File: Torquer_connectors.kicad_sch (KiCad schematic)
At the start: 0 parts

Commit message: eeprom fanned out
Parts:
- added JT1, JT2, JT3: 502352-0210, symbol 502352-0210:502352-0210
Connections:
- new net GND: JT1.MP1, JT1.MP2, JT2.MP1, JT2.MP2, JT3.MP1, JT3.MP2
- new net MT2_Out1: JT2.1
- new net MT2_Out2: JT2.2
- new net MT3_Out1: JT3.1
- new net MT3_Out2: JT3.2
- new net MT_Out1: JT1.1
- new net MT_Out2: JT1.2
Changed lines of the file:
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@@
 (kicad_sch (version 20211123) (generator eeschema)
   (paper "A4")
+  (junction (at 36.83 58.42) (diameter 0) (color 0 0 0 0)
+  )
+  (junction (at 35.56 34.29) (diameter 0) (color 0 0 0 0)
+  )
+  (junction (at 39.37 85.09) (diameter 0) (color 0 0 0 0)
+  )
+  (wire (pts (xy 39.37 85.09) (xy 39.37 87.63))
+    (stroke (width 0) (type default) (color 0 0 0 0))
+  )
+  (wire (pts (xy 36.83 58.42) (xy 39.37 58.42))
+    (stroke (width 0) (type default) (color 0 0 0 0))
+  )
+  (wire (pts (xy 35.56 34.29) (xy 39.37 34.29))
+    (stroke (width 0) (type default) (color 0 0 0 0))
+  )
+  (wire (pts (xy 39.37 31.75) (xy 35.56 31.75))
+    (stroke (width 0) (type default) (color 0 0 0 0))
+  )
+  (wire (pts (xy 36.83 58.42) (xy 36.83 62.23))
+    (stroke (width 0) (type default) (color 0 0 0 0))
+  )
+  (wire (pts (xy 39.37 85.09) (xy 40.64 85.09))
+    (stroke (width 0) (type default) (color 0 0 0 0))
+  )
+  (wire (pts (xy 35.56 31.75) (xy 35.56 34.29))
+    (stroke (width 0) (type default) (color 0 0 0 0))
+  )
+  (wire (pts (xy 40.64 82.55) (xy 39.37 82.55))
+    (stroke (width 0) (type default) (color 0 0 0 0))
+  )
+  (wire (pts (xy 36.83 55.88) (xy 36.83 58.42))
+    (stroke (width 0) (type default) (color 0 0 0 0))
+  )
+  (wire (pts (xy 39.37 82.55) (xy 39.37 85.09))
+    (stroke (width 0) (type default) (color 0 0 0 0))
+  )
+  (wire (pts (xy 39.37 55.88) (xy 36.83 55.88))
+    (stroke (width 0) (type default) (color 0 0 0 0))
+  )
+  (wire (pts (xy 35.56 34.29) (xy 35.56 35.56))
+    (stroke (width 0) (type default) (color 0 0 0 0))
+  )
+  (hierarchical_label "MT_Out1" (shape input) (at 62.23 31.75 0)
+    (effects (font (size 1.27 1.27)) (justify left))
+  )
+  (hierarchical_label "MT3_Out1" (shape input) (at 63.5 82.55 0)
+    (effects (font (size 1.27 1.27)) (justify left))
+  )
+  (hierarchical_label "MT2_Out1" (shape input) (at 62.23 55.88 0)
+    (effects (font (size 1.27 1.27)) (justify left))
+  )
+  (hierarchical_label "MT_Out2" (shape input) (at 62.23 34.29 0)
+    (effects (font (size 1.27 1.27)) (justify left))
+  )
+  (hierarchical_label "MT3_Out2" (shape input) (at 63.5 85.09 0)
+    (effects (font (size 1.27 1.27)) (justify left))
+  )
+  (hierarchical_label "MT2_Out2" (shape input) (at 62.23 58.42 0)
+    (effects (font (size 1.27 1.27)) (justify left))
+  )
+  (symbol (lib_id "power:GND") (at 36.83 62.23 0) (unit 1)
+    (in_bom yes) (on_board yes) (fields_autoplaced)
+    (property "Reference" "#PWR?" (id 0) (at 36.83 68.58 0)
+      (effects (font (size 1.27 1.27)) hide)
+    )
+    (property "Value" "GND" (id 1) (at 36.83 67.31 0))
+    (property "Footprint" "" (id 2) (at 36.83 62.23 0)
+      (effects (font (size 1.27 1.27)) hide)
+    )
+    (property "Datasheet" "" (id 3) (at 36.83 62.23 0)
+      (effects (font (size 1.27 1.27)) hide)
+    )
+    (pin "1")
+  )
+  (symbol (lib_id "502352-0210:502352-0210") (at 39.37 55.88 0) (unit 1)
+    (in_bom yes) (on_board yes) (fields_autoplaced)
+    (property "Reference" "JT2" (id 0) (at 50.8 43.18 0))
+    (property "Value" "502352-0210" (id 1) (at 50.8 45.72 0))
+    (property "Footprint" "" (id 2) (at 39.37 55.88 0)
+      (effects (font (size 1.27 1.27)) hide)
+    )
+    (property "Datasheet" "" (id 3) (at 39.37 55.88 0)
+      (effects (font (size 1.27 1.27)) hide)
+    )
+    (property "Reference_1" "J" (id 4) (at 50.8 48.26 0))
+    (property "Value_1" "502352-0210" (id 5) (at 50.8 50.8 0))
+    (property "Footprint_1" "5023520210" (id 6) (at 58.42 150.8 0)
+      (effects (font (size 1.27 1.27)) (justify left top) hide)
+    )
+    (property "Datasheet_1" "https://componentsearchengine.com/Datasheets/1/502352-0210.pdf" (id 7) (at 58.42 250.8 0)
+      (effects (font (size 1.27 1.27)) (justify left top) hide)
+    )
+    (property "Height" "6.4" (id 8) (at 58.42 450.8 0)
+      (effects (font (size 1.27 1.27)) (justify left top) hide)
+    )
+    (property "Mouser Part Number" "538-502352-0210" (id 9) (at 58.42 550.8 0)
+      (effects (font (size 1.27 1.27)) (justify left top) hide)
+    )
+    (property "Mouser Price/Stock" "https://www.mouser.co.uk/ProductDetail/Molex/502352-0210?qs=yd8XiKYcH9lys38VlWdUCA%3D%3D" (id 10) (at 58.42 650.8 0)
+      (effects (font (size 1.27 1.27)) (justify left top) hide)
+    )
+    (property "Manufacturer_Name" "Molex" (id 11) (at 58.42 750.8 0)
+      (effects (font (size 1.27 1.27)) (justify left top) hide)
+    )
+    (property "Manufacturer_Part_Number" "502352-0210" (id 12) (at 58.42 850.8 0)
+      (effects (font (size 1.27 1.27)) (justify left top) hide)
+    )
+    (pin "1")
+    (pin "2")
+    (pin "MP1")
+    (pin "MP2")
+  )
+  (symbol (lib_id "power:GND") (at 39.37 87.63 0) (unit 1)
+    (in_bom yes) (on_board yes) (fields_autoplaced)
+    (property "Reference" "#PWR?" (id 0) (at 39.37 93.98 0)
+      (effects (font (size 1.27 1.27)) hide)
+    )
+    (property "Value" "GND" (id 1) (at 39.37 92.71 0))
+    (property "Footprint" "" (id 2) (at 39.37 87.63 0)
+      (effects (font (size 1.27 1.27)) hide)
+    )
+    (property "Datasheet" "" (id 3) (at 39.37 87.63 0)
+      (effects (font (size 1.27 1.27)) hide)
+    )
+    (pin "1")
+  )
+  (symbol (lib_id "502352-0210:502352-0210") (at 39.37 31.75 0) (unit 1)
+    (in_bom yes) (on_board yes) (fields_autoplaced)
+    (property "Reference" "JT1" (id 0) (at 50.8 19.05 0))
+    (property "Value" "502352-0210" (id 1) (at 50.8 21.59 0))
+    (property "Footprint" "" (id 2) (at 39.37 31.75 0)
+      (effects (font (size 1.27 1.27)) hide)
+    )
+    (property "Datasheet" "" (id 3) (at 39.37 31.75 0)
+      (effects (font (size 1.27 1.27)) hide)
+    )
+    (property "Reference_1" "J" (id 4) (at 50.8 24.13 0))
+    (property "Value_1" "502352-0210" (id 5) (at 50.8 26.67 0))
+    (property "Footprint_1" "5023520210" (id 6) (at 58.42 126.67 0)
+      (effects (font (size 1.27 1.27)) (justify left top) hide)
+    )
+    (property "Datasheet_1" "https://componentsearchengine.com/Datasheets/1/502352-0210.pdf" (id 7) (at 58.42 226.67 0)
+      (effects (font (size 1.27 1.27)) (justify left top) hide)
+    )
+    (property "Height" "6.4" (id 8) (at 58.42 426.67 0)
+      (effects (font (size 1.27 1.27)) (justify left top) hide)
+    )
+    (property "Mouser Part Number" "538-502352-0210" (id 9) (at 58.42 526.67 0)
+      (effects (font (size 1.27 1.27)) (justify left top) hide)
+    )
+    (property "Mouser Price/Stock" "https://www.mouser.co.uk/ProductDetail/Molex/502352-0210?qs=yd8XiKYcH9lys38VlWdUCA%3D%3D" (id 10) (at 58.42 626.67 0)
+      (effects (font (size 1.27 1.27)) (justify left top) hide)
+    )
+    (property "Manufacturer_Name" "Molex" (id 11) (at 58.42 726.67 0)
+      (effects (font (size 1.27 1.27)) (justify left top) hide)
+    )
+    (property "Manufacturer_Part_Number" "502352-0210" (id 12) (at 58.42 826.67 0)
+      (effects (font (size 1.27 1.27)) (justify left top) hide)
+    )
+    (pin "1")
+    (pin "2")
+    (pin "MP1")
+    (pin "MP2")
+  )
+  (symbol (lib_id "power:GND") (at 35.56 35.56 0) (unit 1)
+    (in_bom yes) (on_board yes) (fields_autoplaced)
+    (property "Reference" "#PWR?" (id 0) (at 35.56 41.91 0)
+      (effects (font (size 1.27 1.27)) hide)
+    )
+    (property "Value" "GND" (id 1) (at 35.56 40.64 0))
+    (property "Footprint" "" (id 2) (at 35.56 35.56 0)
+      (effects (font (size 1.27 1.27)) hide)
+    )
+    (property "Datasheet" "" (id 3) (at 35.56 35.56 0)
+      (effects (font (size 1.27 1.27)) hide)
+    )
+    (pin "1")
+  )
+  (symbol (lib_id "502352-0210:502352-0210") (at 40.64 82.55 0) (unit 1)
+    (in_bom yes) (on_board yes) (fields_autoplaced)
+    (property "Reference" "JT3" (id 0) (at 52.07 69.85 0))
+    (property "Value" "502352-0210" (id 1) (at 52.07 72.39 0))
+    (property "Footprint" "" (id 2) (at 40.64 82.55 0)
+      (effects (font (size 1.27 1.27)) hide)
+    )
+    (property "Datasheet" "" (id 3) (at 40.64 82.55 0)
+      (effects (font (size 1.27 1.27)) hide)
+    )
+    (property "Reference_1" "J" (id 4) (at 52.07 74.93 0))
+    (property "Value_1" "502352-0210" (id 5) (at 52.07 77.47 0))
+    (property "Footprint_1" "5023520210" (id 6) (at 59.69 177.47 0)
+      (effects (font (size 1.27 1.27)) (justify left top) hide)
+    )
+    (property "Datasheet_1" "https://componentsearchengine.com/Datasheets/1/502352-0210.pdf" (id 7) (at 59.69 277.47 0)
+      (effects (font (size 1.27 1.27)) (justify left top) hide)
+    )
+    (property "Height" "6.4" (id 8) (at 59.69 477.47 0)
+      (effects (font (size 1.27 1.27)) (justify left top) hide)
+    )
+    (property "Mouser Part Number" "538-502352-0210" (id 9) (at 59.69 577.47 0)
+      (effects (font (size 1.27 1.27)) (justify left top) hide)
+    )
+    (property "Mouser Price/Stock" "https://www.mouser.co.uk/ProductDetail/Molex/502352-0210?qs=yd8XiKYcH9lys38VlWdUCA%3D%3D" (id 10) (at 59.69 677.47 0)
+      (effects (font (size 1.27 1.27)) (justify left top) hide)
+    )
+    (property "Manufacturer_Name" "Molex" (id 11) (at 59.69 777.47 0)
+      (effects (font (size 1.27 1.27)) (justify left top) hide)
+    )
+    (property "Manufacturer_Part_Number" "502352-0210" (id 12) (at 59.69 877.47 0)
+      (effects (font (size 1.27 1.27)) (justify left top) hide)
+    )
+    (pin "1")
+    (pin "2")
+    (pin "MP1")
+    (pin "MP2")
+  )
 )

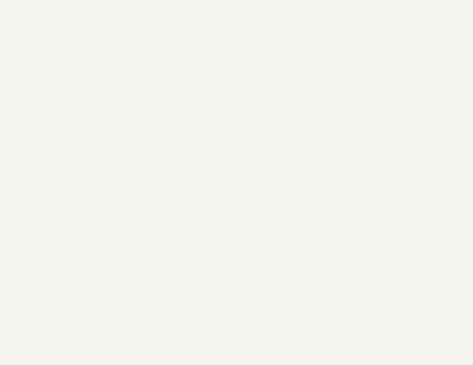
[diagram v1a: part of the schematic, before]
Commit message: MCU interfaces are done! Check the Changes and Complete ERC modifications
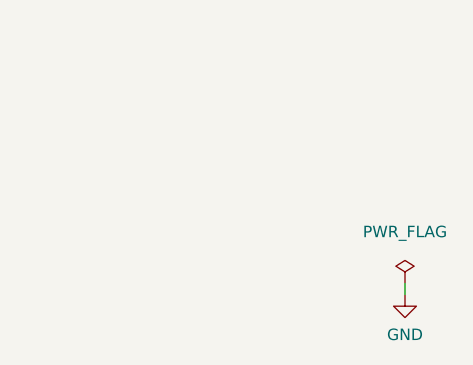
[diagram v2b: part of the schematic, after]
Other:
- company: (none) -> Parikshit Student Satellite Team
- title: (none) -> AOCS BOARD
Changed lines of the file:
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@@
 (kicad_sch (version 20211123) (generator eeschema)
   (paper "A4")
+  (title_block
+    (title "AOCS BOARD")
+    (company "Parikshit Student Satellite Team")
+  )
   (junction (at 36.83 58.42) (diameter 0) (color 0 0 0 0)
   )
@@
     (stroke (width 0) (type default) (color 0 0 0 0))
   )
+  (wire (pts (xy 260.985 143.51) (xy 260.985 142.24))
+    (stroke (width 0) (type default) (color 0 0 0 0))
+  )
   (wire (pts (xy 36.83 58.42) (xy 36.83 62.23))
     (stroke (width 0) (type default) (color 0 0 0 0))
@@
   (symbol (lib_id "power:GND") (at 36.83 62.23 0) (unit 1)
     (in_bom yes) (on_board yes) (fields_autoplaced)
-    (property "Reference" "#PWR?" (id 0) (at 36.83 68.58 0)
+    (property "Reference" "#PWR0247" (id 0) (at 36.83 68.58 0)
       (effects (font (size 1.27 1.27)) hide)
     )
@@
     )
     (property "Datasheet" "" (id 3) (at 36.83 62.23 0)
+      (effects (font (size 1.27 1.27)) hide)
+    )
+    (pin "1")
+  )
+  (symbol (lib_id "power:PWR_FLAG") (at 260.985 142.24 0) (unit 1)
+    (in_bom yes) (on_board yes) (fields_autoplaced)
+    (property "Reference" "#FLG0113" (id 0) (at 260.985 140.335 0)
+      (effects (font (size 1.27 1.27)) hide)
+    )
+    (property "Value" "PWR_FLAG" (id 1) (at 260.985 136.525 0))
+    (property "Footprint" "" (id 2) (at 260.985 142.24 0)
+      (effects (font (size 1.27 1.27)) hide)
+    )
+    (property "Datasheet" "~" (id 3) (at 260.985 142.24 0)
       (effects (font (size 1.27 1.27)) hide)
     )
@@
   (symbol (lib_id "power:GND") (at 39.37 87.63 0) (unit 1)
     (in_bom yes) (on_board yes) (fields_autoplaced)
-    (property "Reference" "#PWR?" (id 0) (at 39.37 93.98 0)
+    (property "Reference" "#PWR0245" (id 0) (at 39.37 93.98 0)
       (effects (font (size 1.27 1.27)) hide)
     )
@@
   (symbol (lib_id "power:GND") (at 35.56 35.56 0) (unit 1)
     (in_bom yes) (on_board yes) (fields_autoplaced)
-    (property "Reference" "#PWR?" (id 0) (at 35.56 41.91 0)
+    (property "Reference" "#PWR0246" (id 0) (at 35.56 41.91 0)
       (effects (font (size 1.27 1.27)) hide)
     )
@@
     (pin "MP2")
   )
+  (symbol (lib_id "power:GND") (at 260.985 143.51 0) (unit 1)
+    (in_bom yes) (on_board yes) (fields_autoplaced)
+    (property "Reference" "#PWR0277" (id 0) (at 260.985 149.86 0)
+      (effects (font (size 1.27 1.27)) hide)
+    )
+    (property "Value" "GND" (id 1) (at 260.985 147.955 0))
+    (property "Footprint" "" (id 2) (at 260.985 143.51 0)
+      (effects (font (size 1.27 1.27)) hide)
+    )
+    (property "Datasheet" "" (id 3) (at 260.985 143.51 0)
+      (effects (font (size 1.27 1.27)) hide)
+    )
+    (pin "1")
+  )
 )

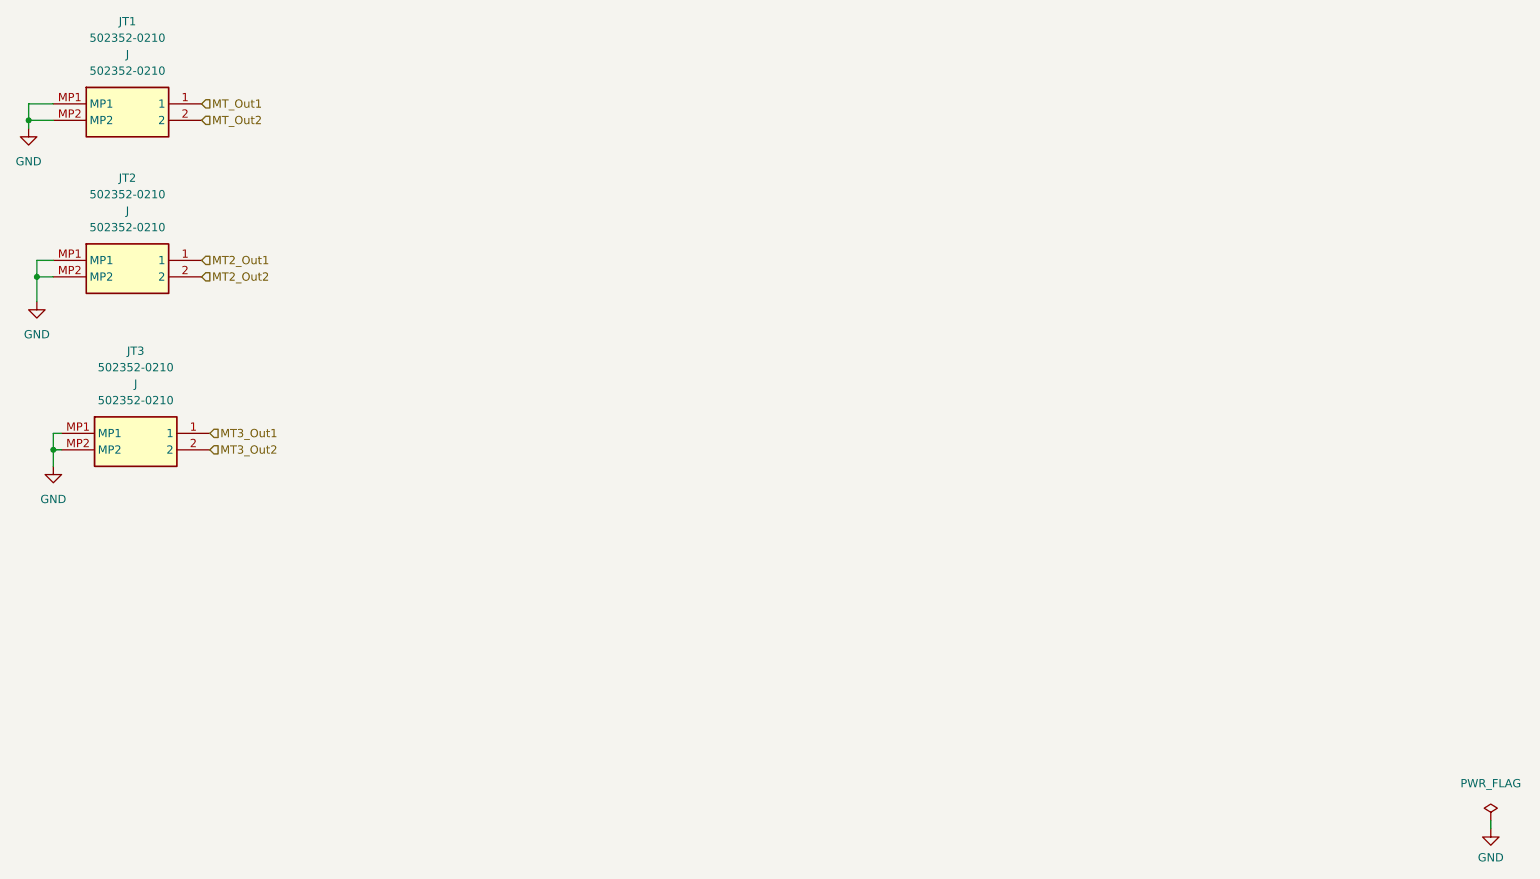
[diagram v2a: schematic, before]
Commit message: Max ERC errors corrected
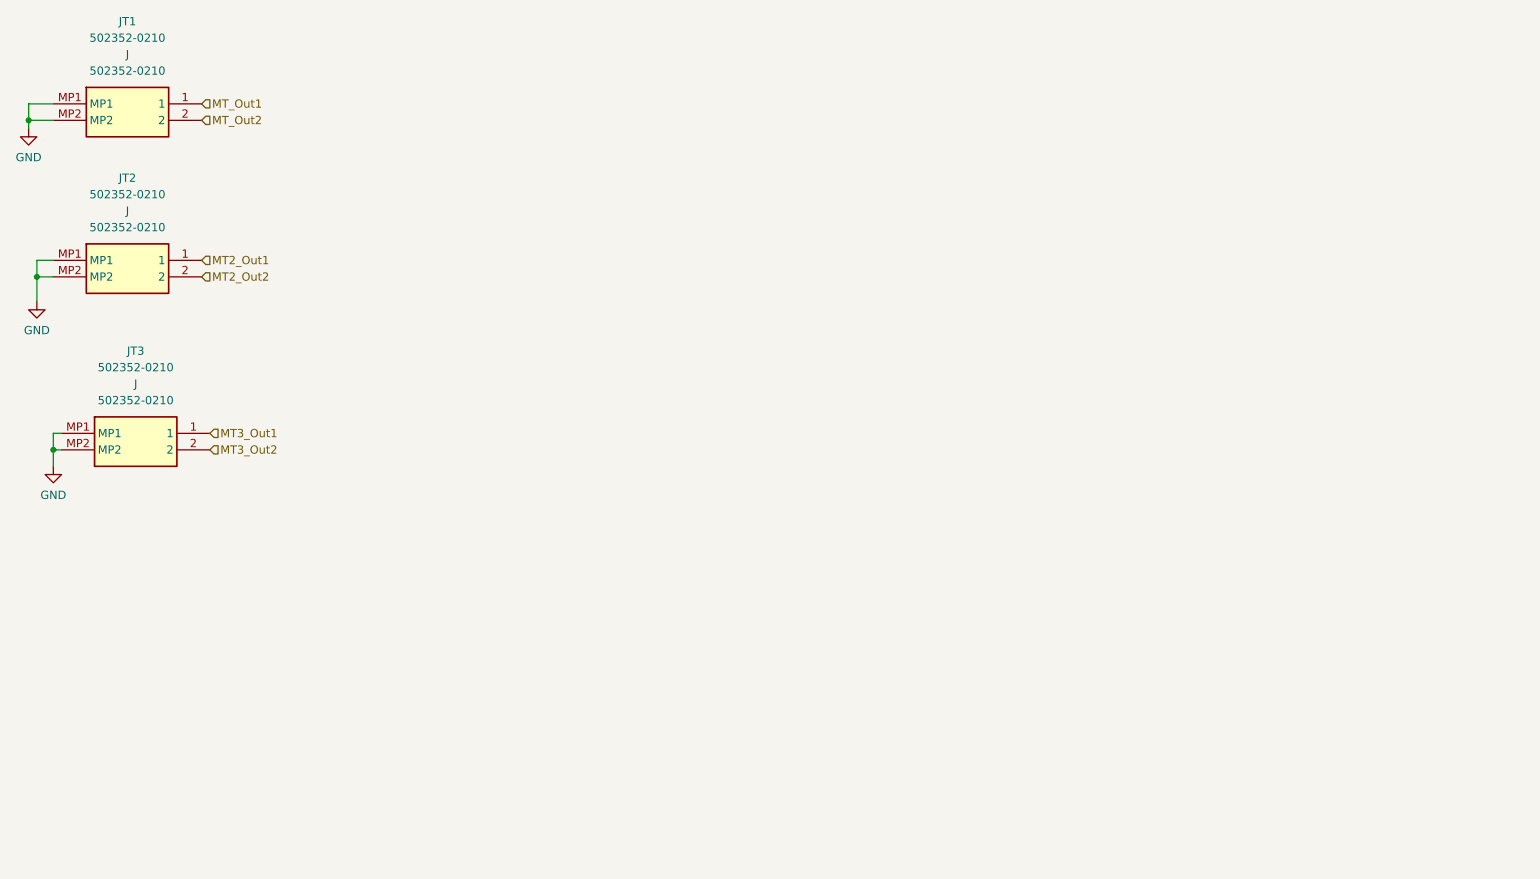
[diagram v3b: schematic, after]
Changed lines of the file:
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@@
-    (stroke (width 0) (type default) (color 0 0 0 0))
-  )
-  (wire (pts (xy 260.985 143.51) (xy 260.985 142.24))
     (stroke (width 0) (type default) (color 0 0 0 0))
   )
@@
     (effects (font (size 1.27 1.27)) (justify left))
   )
-  (symbol (lib_id "power:GND") (at 36.83 62.23 0) (unit 1)
-    (in_bom yes) (on_board yes) (fields_autoplaced)
-    (property "Reference" "#PWR0247" (id 0) (at 36.83 68.58 0)
-      (effects (font (size 1.27 1.27)) hide)
-    )
-    (property "Value" "GND" (id 1) (at 36.83 67.31 0))
-    (property "Footprint" "" (id 2) (at 36.83 62.23 0)
-      (effects (font (size 1.27 1.27)) hide)
-    )
-    (property "Datasheet" "" (id 3) (at 36.83 62.23 0)
-      (effects (font (size 1.27 1.27)) hide)
-    )
-    (pin "1")
-  )
-  (symbol (lib_id "power:PWR_FLAG") (at 260.985 142.24 0) (unit 1)
-    (in_bom yes) (on_board yes) (fields_autoplaced)
-    (property "Reference" "#FLG0113" (id 0) (at 260.985 140.335 0)
-      (effects (font (size 1.27 1.27)) hide)
-    )
-    (property "Value" "PWR_FLAG" (id 1) (at 260.985 136.525 0))
-    (property "Footprint" "" (id 2) (at 260.985 142.24 0)
-      (effects (font (size 1.27 1.27)) hide)
-    )
-    (property "Datasheet" "~" (id 3) (at 260.985 142.24 0)
-      (effects (font (size 1.27 1.27)) hide)
-    )
-    (pin "1")
-  )
   (symbol (lib_id "502352-0210:502352-0210") (at 39.37 55.88 0) (unit 1)
     (in_bom yes) (on_board yes) (fields_autoplaced)
@@
     (pin "MP1")
     (pin "MP2")
-  )
-  (symbol (lib_id "power:GND") (at 39.37 87.63 0) (unit 1)
-    (in_bom yes) (on_board yes) (fields_autoplaced)
-    (property "Reference" "#PWR0245" (id 0) (at 39.37 93.98 0)
-      (effects (font (size 1.27 1.27)) hide)
-    )
-    (property "Value" "GND" (id 1) (at 39.37 92.71 0))
-    (property "Footprint" "" (id 2) (at 39.37 87.63 0)
-      (effects (font (size 1.27 1.27)) hide)
-    )
-    (property "Datasheet" "" (id 3) (at 39.37 87.63 0)
-      (effects (font (size 1.27 1.27)) hide)
-    )
-    (pin "1")
   )
   (symbol (lib_id "502352-0210:502352-0210") (at 39.37 31.75 0) (unit 1)
@@
     (pin "MP2")
   )
-  (symbol (lib_id "power:GND") (at 35.56 35.56 0) (unit 1)
+  (symbol (lib_id "upsat-comms-hardware:GND") (at 36.83 62.23 0) (unit 1)
     (in_bom yes) (on_board yes) (fields_autoplaced)
-    (property "Reference" "#PWR0246" (id 0) (at 35.56 41.91 0)
+    (property "Reference" "#PWR0233" (id 0) (at 36.83 68.58 0)
       (effects (font (size 1.27 1.27)) hide)
     )
-    (property "Value" "GND" (id 1) (at 35.56 40.64 0))
-    (property "Footprint" "" (id 2) (at 35.56 35.56 0)
-      (effects (font (size 1.27 1.27)) hide)
-    )
-    (property "Datasheet" "" (id 3) (at 35.56 35.56 0)
-      (effects (font (size 1.27 1.27)) hide)
-    )
+    (property "Value" "GND" (id 1) (at 36.83 66.675 0))
+    (property "Footprint" "" (id 2) (at 36.83 62.23 0))
+    (property "Datasheet" "" (id 3) (at 36.83 62.23 0))
     (pin "1")
   )
@@
     (pin "MP2")
   )
-  (symbol (lib_id "power:GND") (at 260.985 143.51 0) (unit 1)
+  (symbol (lib_id "upsat-comms-hardware:GND") (at 35.56 35.56 0) (unit 1)
     (in_bom yes) (on_board yes) (fields_autoplaced)
-    (property "Reference" "#PWR0277" (id 0) (at 260.985 149.86 0)
+    (property "Reference" "#PWR0234" (id 0) (at 35.56 41.91 0)
       (effects (font (size 1.27 1.27)) hide)
     )
-    (property "Value" "GND" (id 1) (at 260.985 147.955 0))
-    (property "Footprint" "" (id 2) (at 260.985 143.51 0)
+    (property "Value" "GND" (id 1) (at 35.56 40.005 0))
+    (property "Footprint" "" (id 2) (at 35.56 35.56 0))
+    (property "Datasheet" "" (id 3) (at 35.56 35.56 0))
+    (pin "1")
+  )
+  (symbol (lib_id "upsat-comms-hardware:GND") (at 39.37 87.63 0) (unit 1)
+    (in_bom yes) (on_board yes) (fields_autoplaced)
+    (property "Reference" "#PWR0232" (id 0) (at 39.37 93.98 0)
       (effects (font (size 1.27 1.27)) hide)
     )
-    (property "Datasheet" "" (id 3) (at 260.985 143.51 0)
-      (effects (font (size 1.27 1.27)) hide)
-    )
+    (property "Value" "GND" (id 1) (at 39.37 92.075 0))
+    (property "Footprint" "" (id 2) (at 39.37 87.63 0))
+    (property "Datasheet" "" (id 3) (at 39.37 87.63 0))
     (pin "1")
   )
